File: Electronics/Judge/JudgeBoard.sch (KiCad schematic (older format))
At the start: 4 parts

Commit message: Initial shift-register based judge controller schematic
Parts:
- added SW? (x10): SW_Push, symbol SW_Push
- U? (x2): symbol 74LS166 -> 74LS166-RESCUE-JudgeBoard
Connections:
- net labels added: +3.3V, GND
- wire segments 6 -> 64

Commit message: Updated symbols and footprints for pushbutton
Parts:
- removed RN? (x2): R_Network08, Resistors_THT:R_Array_SIP9, symbol R_Network08
- removed SW? (x10): SW_Push, symbol SW_Push
- removed U? (x2): 74LS166, symbol 74LS166-RESCUE-JudgeBoard
- added C1, C2: C, Capacitors_THT:C_Disc_D3.4mm_W2.1mm_P2.50mm, symbol C
- added C3: CP1, Capacitors_THT:CP_Axial_L11.0mm_D5.0mm_P18.00mm_Horizontal, symbol CP1
- added J1: RJ12-UNSHLD, Pin_Headers:Pin_Header_Straight_2x03_Pitch2.54mm, symbol RJ12-UNSHLD
- added RN1: R_Network10, Resistors_THT:Resistor_Array_SIP11, symbol R_Network10
- added S1, S10, S2, S3, S4, S5, S6, S7, S8, S9: DPDT-Button, Buttons_Switches_THT:MHPS2285V, symbol DPDT-Button
- added U1, U2: 74HC165, Housings_DIP:DIP-16_W7.62mm_LongPads, symbol 74HC165
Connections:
- net labels added: CLK, LOAD
- wire segments 64 -> 80
- no-connect marks 0 -> 43

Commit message: UPdated judge board layout
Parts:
- S1: value DPDT-Button -> R1
- S10: value DPDT-Button -> B5
- S2: value DPDT-Button -> R3
- S3: value DPDT-Button -> R5
- S4: value DPDT-Button -> B2
- S5: value DPDT-Button -> B4
- S6: value DPDT-Button -> R2
- S7: value DPDT-Button -> R4
- S8: value DPDT-Button -> B1
- S9: value DPDT-Button -> B3
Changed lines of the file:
@@
 P 1300 2200
 F 0 "S1" H 1300 2650 60  0000 C CNN
-F 1 "DPDT-Button" H 1300 2200 60  0000 C CNN
+F 1 "R1" H 1300 2200 60  0000 C CNN
 F 2 "Buttons_Switches_THT:MHPS2285V" H 1300 2200 60  0001 C CNN
 F 3 "" H 1300 2200 60  0001 C CNN
@@
 P 2700 2500
 F 0 "S6" H 2700 2950 60  0000 C CNN
-F 1 "DPDT-Button" H 2700 2500 60  0000 C CNN
+F 1 "R2" H 2700 2500 60  0000 C CNN
 F 2 "Buttons_Switches_THT:MHPS2285V" H 2700 2500 60  0001 C CNN
 F 3 "" H 2700 2500 60  0001 C CNN
@@
 P 1300 3250
 F 0 "S2" H 1300 3700 60  0000 C CNN
-F 1 "DPDT-Button" H 1300 3250 60  0000 C CNN
+F 1 "R3" H 1300 3250 60  0000 C CNN
 F 2 "Buttons_Switches_THT:MHPS2285V" H 1300 3250 60  0001 C CNN
 F 3 "" H 1300 3250 60  0001 C CNN
@@
 P 2700 3550
 F 0 "S7" H 2700 4000 60  0000 C CNN
-F 1 "DPDT-Button" H 2700 3550 60  0000 C CNN
+F 1 "R4" H 2700 3550 60  0000 C CNN
 F 2 "Buttons_Switches_THT:MHPS2285V" H 2700 3550 60  0001 C CNN
 F 3 "" H 2700 3550 60  0001 C CNN
@@
 P 1300 4250
 F 0 "S3" H 1300 4700 60  0000 C CNN
-F 1 "DPDT-Button" H 1300 4250 60  0000 C CNN
+F 1 "R5" H 1300 4250 60  0000 C CNN
 F 2 "Buttons_Switches_THT:MHPS2285V" H 1300 4250 60  0001 C CNN
 F 3 "" H 1300 4250 60  0001 C CNN
@@
 P 2700 4550
 F 0 "S8" H 2700 5000 60  0000 C CNN
-F 1 "DPDT-Button" H 2700 4550 60  0000 C CNN
+F 1 "B1" H 2700 4550 60  0000 C CNN
 F 2 "Buttons_Switches_THT:MHPS2285V" H 2700 4550 60  0001 C CNN
 F 3 "" H 2700 4550 60  0001 C CNN
@@
 P 1300 5300
 F 0 "S4" H 1300 5750 60  0000 C CNN
-F 1 "DPDT-Button" H 1300 5300 60  0000 C CNN
+F 1 "B2" H 1300 5300 60  0000 C CNN
 F 2 "Buttons_Switches_THT:MHPS2285V" H 1300 5300 60  0001 C CNN
 F 3 "" H 1300 5300 60  0001 C CNN
@@
 P 2700 5600
 F 0 "S9" H 2700 6050 60  0000 C CNN
-F 1 "DPDT-Button" H 2700 5600 60  0000 C CNN
+F 1 "B3" H 2700 5600 60  0000 C CNN
 F 2 "Buttons_Switches_THT:MHPS2285V" H 2700 5600 60  0001 C CNN
 F 3 "" H 2700 5600 60  0001 C CNN
@@
 P 1300 6300
 F 0 "S5" H 1300 6750 60  0000 C CNN
-F 1 "DPDT-Button" H 1300 6300 60  0000 C CNN
+F 1 "B4" H 1300 6300 60  0000 C CNN
 F 2 "Buttons_Switches_THT:MHPS2285V" H 1300 6300 60  0001 C CNN
 F 3 "" H 1300 6300 60  0001 C CNN
@@
 P 2700 6600
 F 0 "S10" H 2700 7050 60  0000 C CNN
-F 1 "DPDT-Button" H 2700 6600 60  0000 C CNN
+F 1 "B5" H 2700 6600 60  0000 C CNN
 F 2 "Buttons_Switches_THT:MHPS2285V" H 2700 6600 60  0001 C CNN
 F 3 "" H 2700 6600 60  0001 C CNN

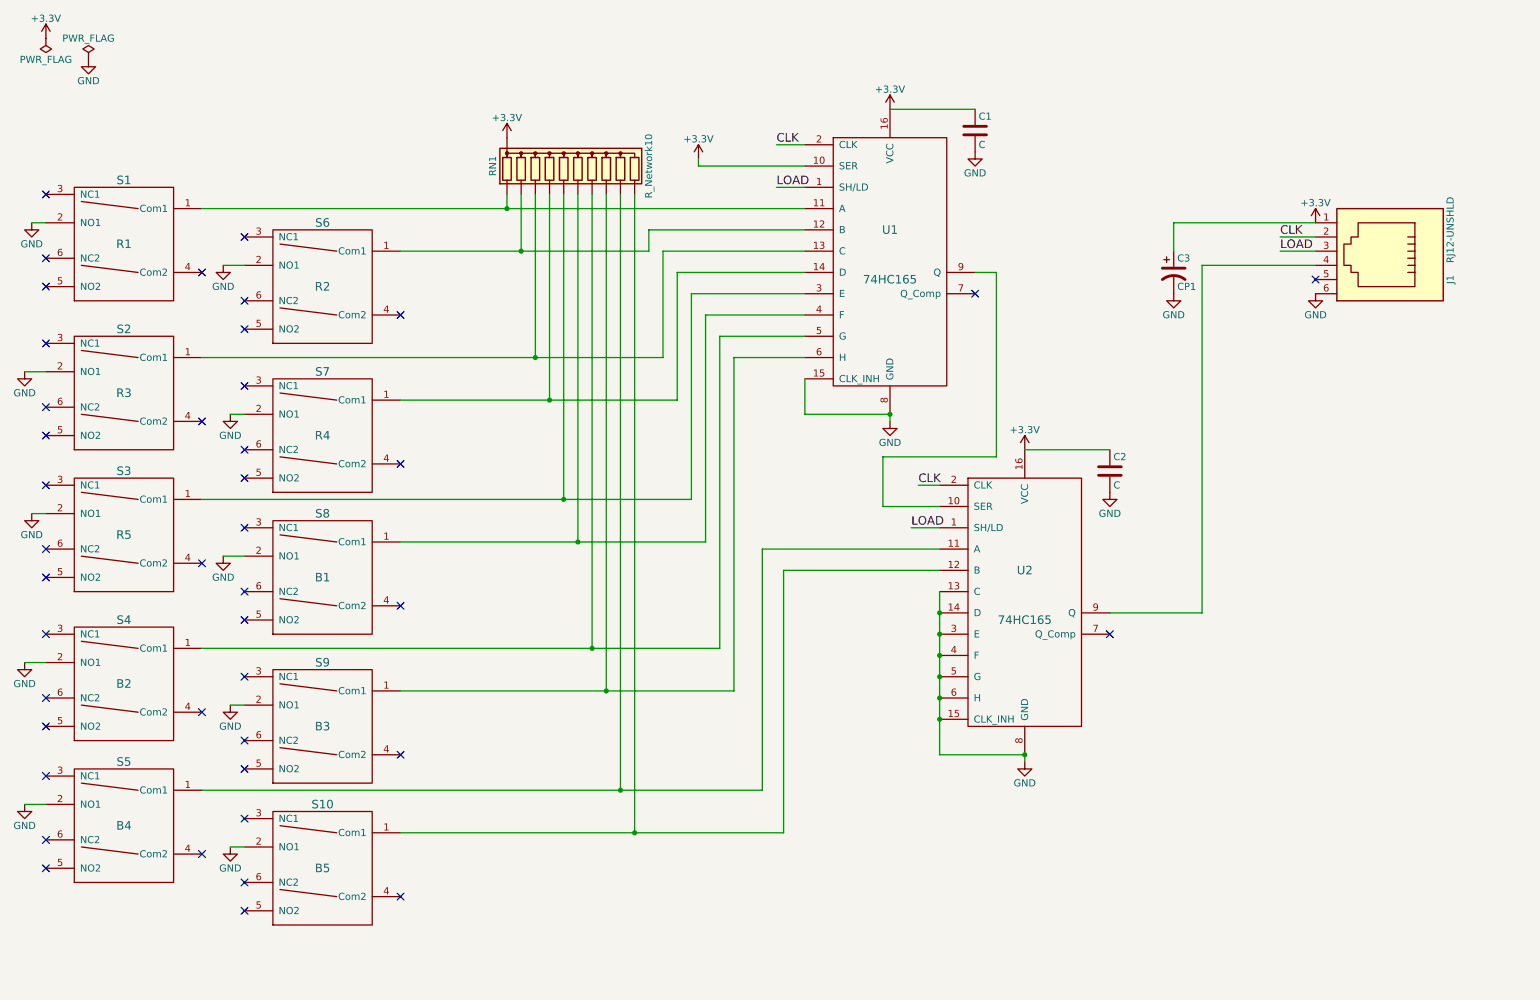
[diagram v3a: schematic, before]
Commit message: Simplified judge controller schematic and pcb
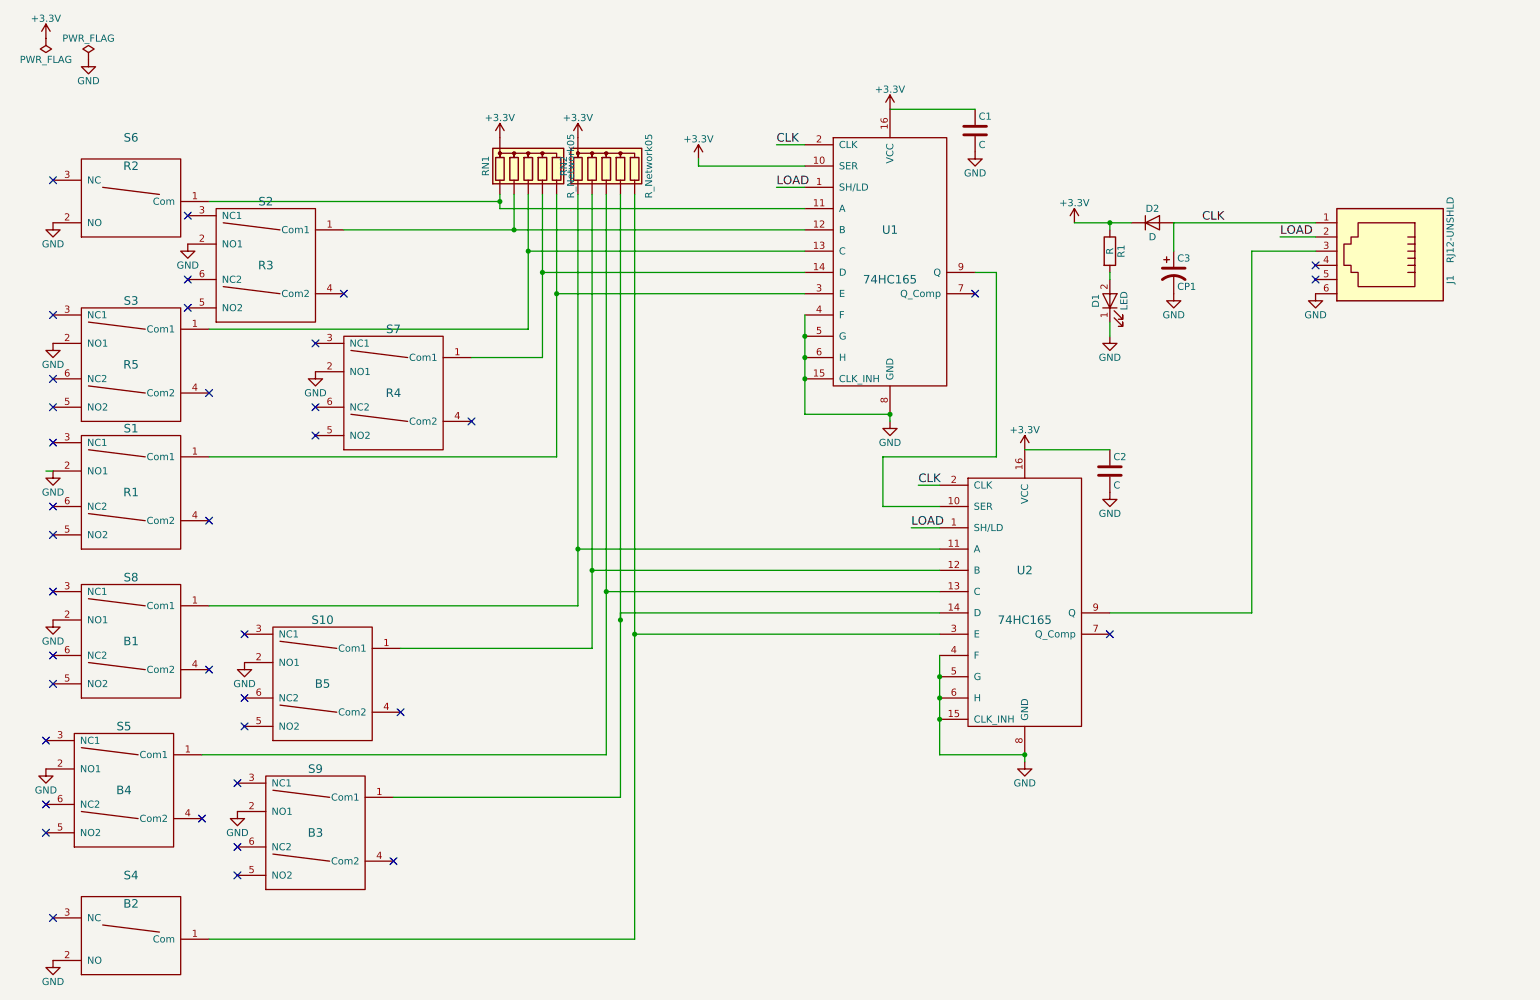
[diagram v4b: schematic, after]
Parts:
- removed RN1: R_Network10, Resistors_THT:Resistor_Array_SIP11, symbol R_Network10
- removed S4: B2, Buttons_Switches_THT:MHPS2285V, symbol DPDT-Button
- removed S6: R2, Buttons_Switches_THT:MHPS2285V, symbol DPDT-Button
- added D1: LED, LEDs:LED_D2.0mm_W4.8mm_H2.5mm_FlatTop, symbol LED
- added D2: D, Diodes_THT:D_DO-35_SOD27_P5.08mm_Vertical_AnodeUp, symbol D
- added R1: R, Resistors_THT:R_Axial_DIN0207_L6.3mm_D2.5mm_P2.54mm_Vertical, symbol R
- added RN1, RN2: R_Network05, Resistors_THT:R_Array_SIP6, symbol R_Network05
- added S4: B2, PiKwonDo:Switch-SPDT, symbol DPST-Button
- added S6: R2, PiKwonDo:Switch-SPDT, symbol DPST-Button
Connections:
- net +3V3: now also D2.1 (K), R1.1, RN1.1 (common), RN2.1 (common); no longer C3.1, J1.1
- net CLK: now also C3.1, J1.1, D2.2 (A); no longer J1.2
- net GND: now also U1.4 (F), U1.5 (G), U1.6 (H), D1.1 (K), S4.2 (NO), S6.2 (NO); no longer U2.13 (C), U2.14 (D), U2.3 (E)
- net LOAD: now also J1.2; no longer J1.3
- net at U1.11 (A): now also RN1.2 (R1), S6.1 (Com); no longer S1.1 (Com1)
- net at U1.12 (B): now also S2.1 (Com1), RN1.3 (R2)
- net at U1.13 (C): now also S3.1 (Com1), RN1.4 (R3); no longer S2.1 (Com1)
- net at S7.1 (Com1), U1.14 (D): now also RN1.5 (R4)
- net at U1.3 (E): now also S1.1 (Com1), RN1.6 (R5); no longer S3.1 (Com1)
- net at S8.1 (Com1): now also U2.11 (A), RN2.2 (R1); no longer U1.4 (F)
- net at S9.1 (Com1): now also U2.14 (D), RN2.5 (R4); no longer U1.6 (H)
- net at S5.1 (Com1): now also U2.13 (C), RN2.4 (R3); no longer U2.11 (A)
- net at S10.1 (Com1), U2.12 (B): now also RN2.3 (R2)
- net at U2.9 (Q): now also J1.3; no longer J1.4
- new net: RN2.6 (R5), S4.1 (Com), U2.3 (E)
- new net: D1.2 (A), R1.2
- no-connect marks 43 -> 38
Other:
- moved on the sheet: S1, S10, S2, S3, S5, S7, S8, S9

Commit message: Updated trace locations
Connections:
- net +3V3: now also C3.1
- net CLK: no longer C3.1
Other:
- moved on the sheet: D2
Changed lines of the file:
@@
 	7650 3650 8250 3650
-Wire Wire Line
-	9700 2050 8700 2050
 Wire Wire Line
 	8700 2050 8700 2250
@@
 	1    0    0    -1
 $EndComp
-Text Label 8900 2050 0    60   ~ 0
+Text Label 9200 2050 0    60   ~ 0
 CLK
 $Comp
 L D D2
 U 1 1 5B2833EA
-P 8550 2050
-F 0 "D2" H 8550 2150 50  0000 C CNN
-F 1 "D" H 8550 1950 50  0000 C CNN
-F 2 "Diodes_THT:D_DO-35_SOD27_P5.08mm_Vertical_AnodeUp" H 8550 2050 50  0001 C CNN
-F 3 "" H 8550 2050 50  0001 C CNN
-	1    8550 2050
+P 8900 2050
+F 0 "D2" H 8900 2150 50  0000 C CNN
+F 1 "D" H 8900 1950 50  0000 C CNN
+F 2 "Diodes_THT:D_DO-35_SOD27_P5.08mm_Vertical_AnodeUp" H 8900 2050 50  0001 C CNN
+F 3 "" H 8900 2050 50  0001 C CNN
+	1    8900 2050
 	1    0    0    -1
 $EndComp
@@
 $EndComp
 Wire Wire Line
-	8000 2050 8400 2050
+	8000 2050 8750 2050
 Wire Wire Line
 	8250 2100 8250 2050
@@
 	4700 5800 1850 5800
 Connection ~ 4700 4650
+Connection ~ 8700 2050
+Wire Wire Line
+	9050 2050 9700 2050
 $EndSCHEMATC

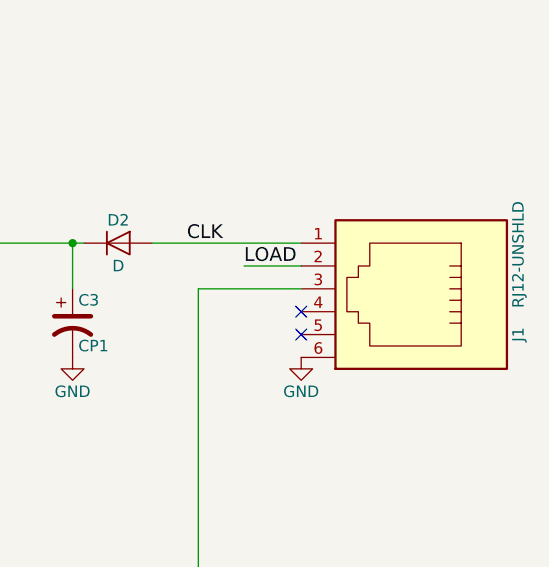
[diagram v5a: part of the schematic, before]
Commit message: Cleaned up judge controller PCB, removed 3 jumpers
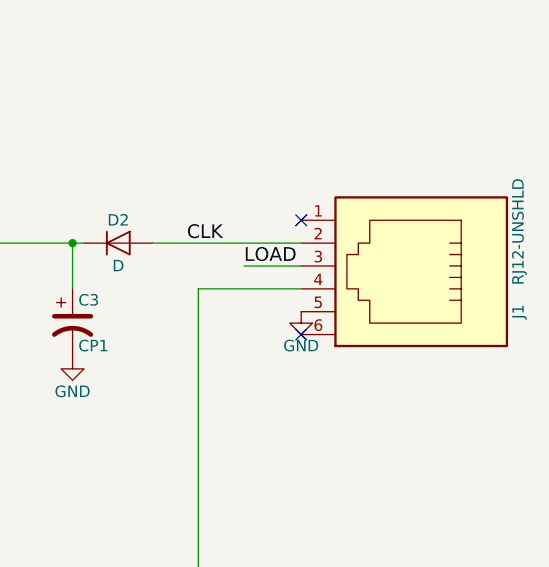
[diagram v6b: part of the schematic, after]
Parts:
- J1: footprint Pin_Headers:Pin_Header_Straight_2x03_Pitch2.54mm -> PiKwonDo:TH-RJ12
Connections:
- net CLK: now also J1.2; no longer J1.1
- net GND: now also J1.5; no longer J1.6
- net LOAD: now also J1.3; no longer J1.2
- net at U2.9 (Q): now also J1.4; no longer J1.3
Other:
- moved on the sheet: J1
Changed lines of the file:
@@
 L RJ12-UNSHLD J1
 U 1 1 5AED1621
-P 10150 2250
-F 0 "J1" H 10350 2750 50  0000 C CNN
-F 1 "RJ12-UNSHLD" H 10000 2750 50  0000 C CNN
-F 2 "Pin_Headers:Pin_Header_Straight_2x03_Pitch2.54mm" H 10150 2250 50  0001 C CNN
-F 3 "" H 10150 2250 50  0001 C CNN
-	1    10150 2250
+P 10150 2150
+F 0 "J1" H 10350 2650 50  0000 C CNN
+F 1 "RJ12-UNSHLD" H 10000 2650 50  0000 C CNN
+F 2 "PiKwonDo:TH-RJ12" H 10150 2150 50  0001 C CNN
+F 3 "" H 10150 2150 50  0001 C CNN
+	1    10150 2150
 	0    1    1    0
 $EndComp
@@
 L GND #PWR09
 U 1 1 5AED1707
-P 9700 2550
-F 0 "#PWR09" H 9700 2300 50  0001 C CNN
-F 1 "GND" H 9700 2400 50  0000 C CNN
-F 2 "" H 9700 2550 50  0001 C CNN
-F 3 "" H 9700 2550 50  0001 C CNN
-	1    9700 2550
+P 9700 2350
+F 0 "#PWR09" H 9700 2100 50  0001 C CNN
+F 1 "GND" H 9700 2200 50  0000 C CNN
+F 2 "" H 9700 2350 50  0001 C CNN
+F 3 "" H 9700 2350 50  0001 C CNN
+	1    9700 2350
 	1    0    0    -1
 $EndComp
@@
 NoConn ~ 7300 2550
 NoConn ~ 8250 4950
-NoConn ~ 9700 2450
 Wire Wire Line
 	6100 2700 6100 3400
@@
 	1    0    0    -1
 $EndComp
-NoConn ~ 9700 2350
 Wire Wire Line
 	3950 1850 3950 1950
@@
 Wire Wire Line
 	9050 2050 9700 2050
+NoConn ~ 9700 2450
+NoConn ~ 9700 1950
 $EndSCHEMATC
